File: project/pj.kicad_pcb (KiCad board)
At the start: 2 copper layers, 65 x 56.5 mm, 11 parts, among them J1 RPi_GPIO, J2 2B+, J3 zero, J4 3A+, J5 3B+, J6 4, J7 Conn_01x02, J8 Conn_01x02, SW1 SW_Push, SW2 SW_Push

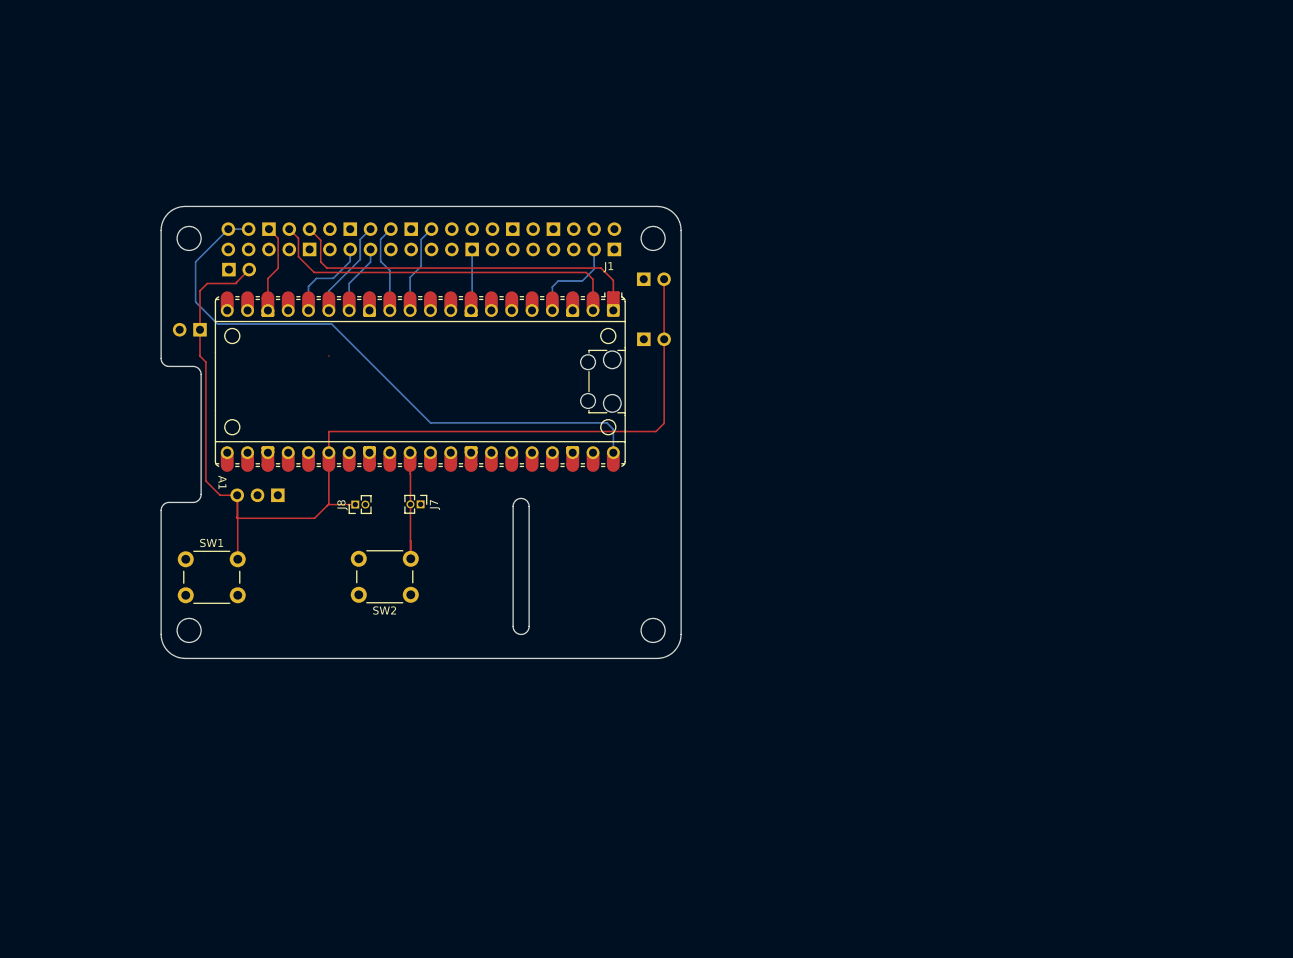
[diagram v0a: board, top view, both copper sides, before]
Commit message: ground plane on both sides
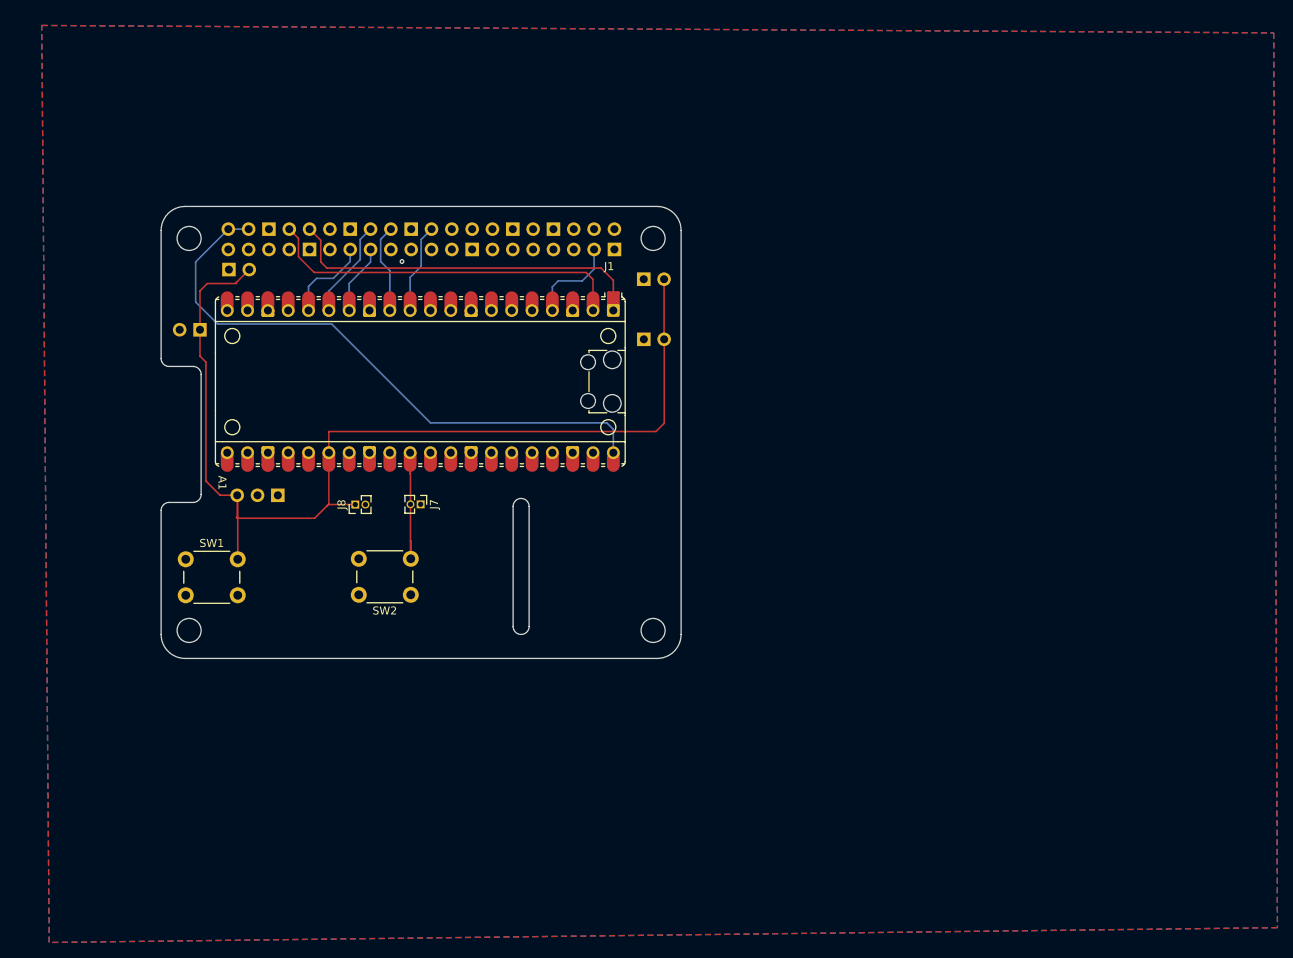
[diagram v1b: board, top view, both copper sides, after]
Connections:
- J1 pad 14: unconnected-(J1-GND-Pad14) -> GND
- J1 pad 20: unconnected-(J1-GND-Pad20) -> GND
- J1 pad 30: unconnected-(J1-GND-Pad30) -> GND
- J1 pad 34: unconnected-(J1-GND-Pad34) -> GND
- J1 pad 9: unconnected-(J1-GND-Pad9) -> GND
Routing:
- net GND: track 18.9 -> 0.19 mm, vias 0 -> 1
- added copper zone on B.Cu, net GND
- added copper zone on F.Cu, net GND

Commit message: pwr eneble
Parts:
- added J10: Pico PWR enable, Jumper:SolderJumper-2_P1.3mm_Bridged2Bar_Pad1.0x1.5mm, F.Cu at (93.0, 77.5)
- added J9: External PWR, Connector_PinHeader_1.27mm:PinHeader_1x02_P1.27mm_Vertical, F.Cu at (93.0, 83.2)
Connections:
- J1 pad 2: Net-(A1-VBUS) -> Net-(J10-Pin_2)
- J1 pad 4: Net-(A1-VBUS) -> Net-(J10-Pin_2)
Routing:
- net Net-(A1-VBUS): track 75.1 -> 6.24 mm
- net Net-(A1-GPIO20): track 132.2 -> 91.3 mm
- net Net-(J10-Pin_2): track 0.00 -> 4.46 mm
- removed copper zone on B.Cu, net GND
- removed copper zone on F.Cu, net GND

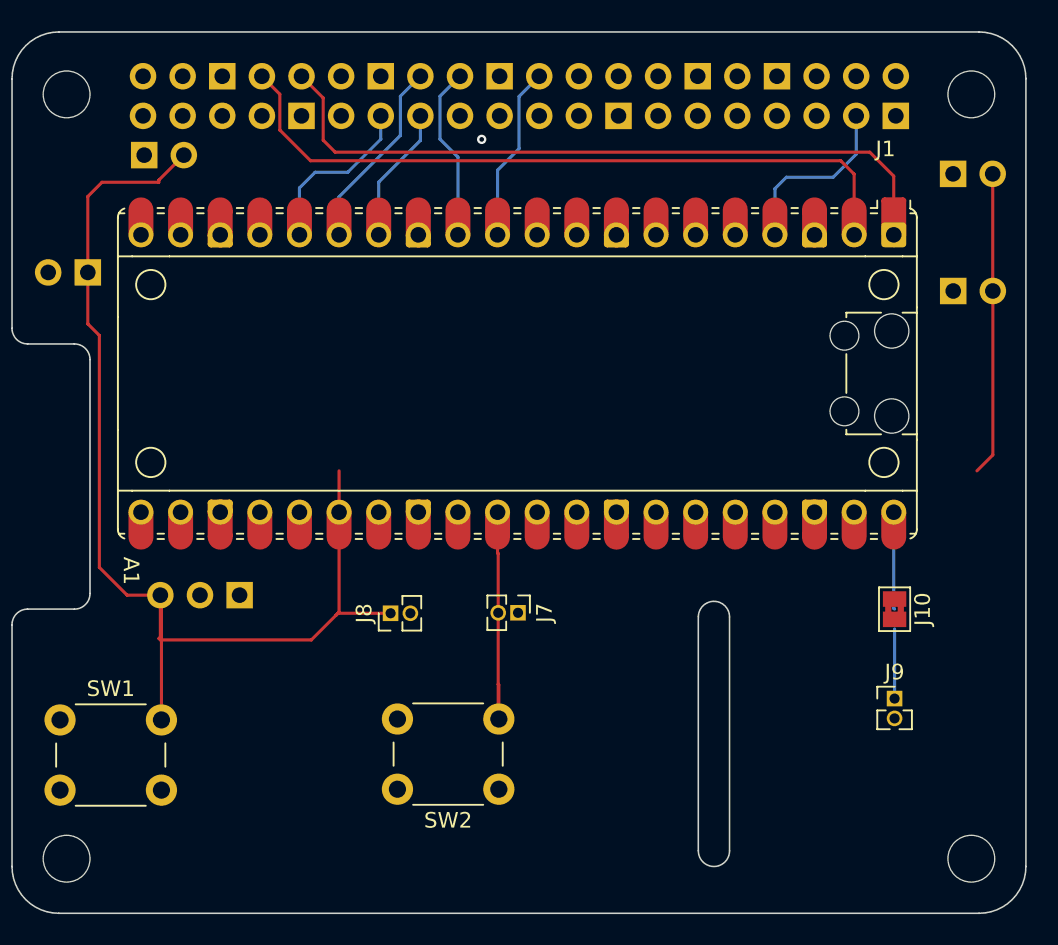
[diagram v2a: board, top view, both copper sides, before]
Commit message: re-route power for more power
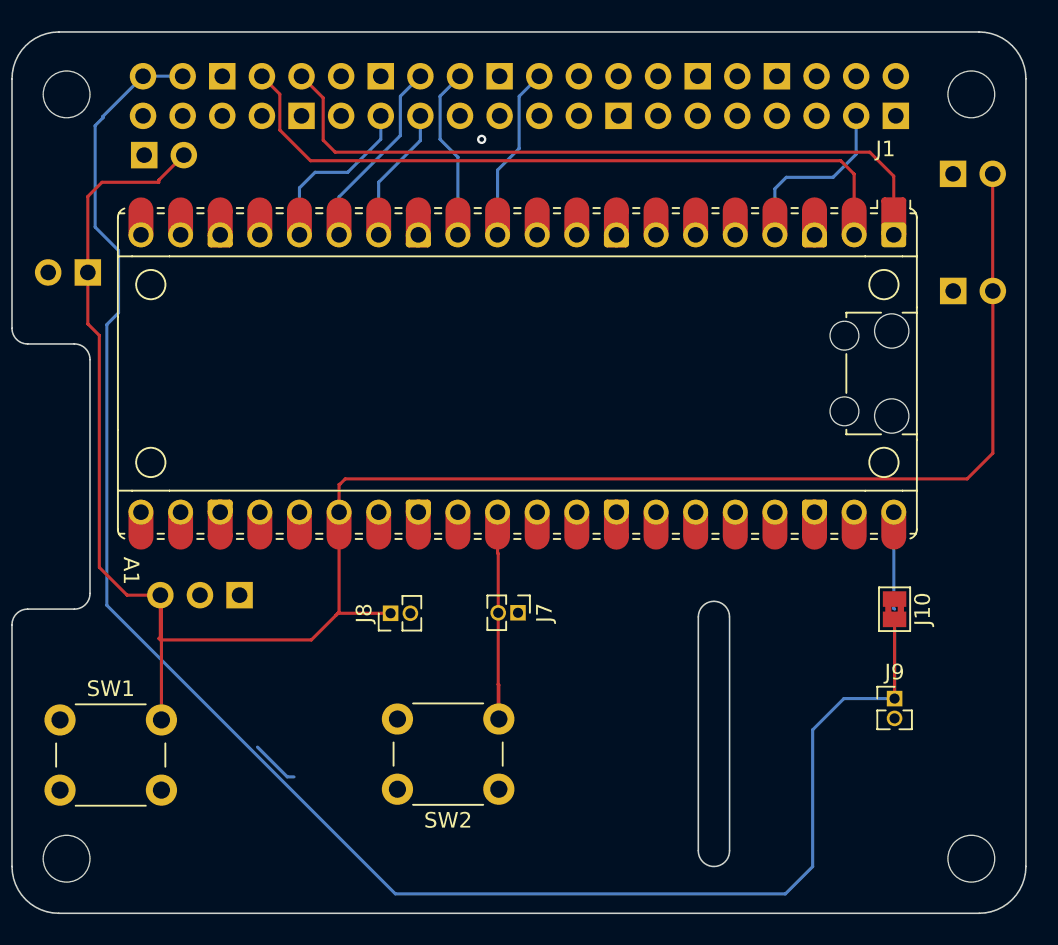
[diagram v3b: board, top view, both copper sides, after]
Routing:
- net Net-(J10-Pin_2): track 4.46 -> 116.7 mm
- net Net-(A1-GPIO20): track 91.3 -> 131.6 mm
- net (no net): track 0.00 -> 3.13 mm
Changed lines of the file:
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@@
 		(fp_arc
 			(start 10.579676 25.189937)
-			(mid 10.35796 25.493961)
+			(mid 10.357949 25.493953)
 			(end 10 25.61)
 			(stroke
@@
 	)
 	(segment
+		(start 54.065686 88.25)
+		(end 52.157843 86.342157)
+		(width 0.2)
+		(layer "B.Cu")
+		(net 0)
+	)
+	(segment
+		(start 54.5 88.25)
+		(end 54.065686 88.25)
+		(width 0.2)
+		(layer "B.Cu")
+		(net 0)
+	)
+	(segment
 		(start 67.46 53.4125)
 		(end 67.5475 53.5)
@@
 	)
 	(segment
+		(start 57.3875 71.28)
+		(end 57.3875 69.5)
+		(width 0.2)
+		(layer "F.Cu")
+		(net 10)
+	)
+	(segment
 		(start 45.93 79.47)
 		(end 45.84 79.38)
@@
 	)
 	(segment
-		(start 57.3875 71.28)
-		(end 57.3875 68.63)
+		(start 55.61 79.47)
+		(end 45.93 79.47)
 		(width 0.2)
 		(layer "F.Cu")
@@
 	)
 	(segment
-		(start 55.61 79.47)
-		(end 45.93 79.47)
+		(start 41.28 55.91)
+		(end 41.28 51.04)
 		(width 0.2)
 		(layer "F.Cu")
@@
 	)
 	(segment
-		(start 41.28 55.91)
-		(end 41.28 51.04)
+		(start 57.783778 69.146278)
+		(end 97.653722 69.146278)
 		(width 0.2)
 		(layer "F.Cu")
@@
 	)
 	(segment
+		(start 57.3875 69.5)
+		(end 57.430056 69.5)
+		(width 0.2)
+		(layer "F.Cu")
+		(net 10)
+	)
+	(segment
+		(start 97.653722 69.146278)
+		(end 99.3 67.5)
+		(width 0.2)
+		(layer "F.Cu")
+		(net 10)
+	)
+	(segment
 		(start 45.83 50.13)
 		(end 45.83 49.995)
@@
 	)
 	(segment
+		(start 99.3 57.1)
+		(end 99.3 67.5)
+		(width 0.2)
+		(layer "F.Cu")
+		(net 10)
+	)
+	(segment
 		(start 41.28 59.21)
 		(end 42.02 59.95)
@@
 	)
 	(segment
-		(start 99.3 57.1)
-		(end 99.3 67.61)
-		(width 0.2)
-		(layer "F.Cu")
-		(net 10)
-	)
-	(segment
 		(start 43.8 76.6)
 		(end 45.93 76.6)
@@
 	)
 	(segment
-		(start 57.3875 77.6925)
-		(end 57.18 77.9)
+		(start 57.430056 69.5)
+		(end 57.783778 69.146278)
 		(width 0.2)
 		(layer "F.Cu")
@@
 	)
 	(segment
-		(start 99.3 67.61)
-		(end 98.28 68.63)
+		(start 57.3875 77.6925)
+		(end 57.18 77.9)
 		(width 0.2)
 		(layer "F.Cu")
@@
 	)
 	(segment
+		(start 93 78.15)
+		(end 93 83.23)
+		(width 0.2)
+		(layer "F.Cu")
+		(net 63)
+	)
+	(segment
+		(start 43.25 58.5)
+		(end 42.5 59.25)
+		(width 0.2)
+		(layer "B.Cu")
+		(net 63)
+	)
+	(segment
+		(start 44.82 43.333)
+		(end 47.36 43.333)
+		(width 0.2)
+		(layer "B.Cu")
+		(net 63)
+	)
+	(segment
+		(start 43.25 54.5)
+		(end 43.25 58.5)
+		(width 0.2)
+		(layer "B.Cu")
+		(net 63)
+	)
+	(segment
+		(start 89.75 83.23)
+		(end 93 83.23)
+		(width 0.2)
+		(layer "B.Cu")
+		(net 63)
+	)
+	(segment
+		(start 41.75 53)
+		(end 43.25 54.5)
+		(width 0.2)
+		(layer "B.Cu")
+		(net 63)
+	)
+	(segment
+		(start 42.25 45.903)
+		(end 42.25 46)
+		(width 0.2)
+		(layer "B.Cu")
+		(net 63)
+	)
+	(segment
+		(start 61 95.75)
+		(end 86 95.75)
+		(width 0.2)
+		(layer "B.Cu")
+		(net 63)
+	)
+	(segment
+		(start 44.82 43.333)
+		(end 42.25 45.903)
+		(width 0.2)
+		(layer "B.Cu")
+		(net 63)
+	)
+	(segment
+		(start 87.75 94)
+		(end 87.75 85.23)
+		(width 0.2)
+		(layer "B.Cu")
+		(net 63)
+	)
+	(segment
+		(start 87.75 85.23)
+		(end 89.75 83.23)
+		(width 0.2)
+		(layer "B.Cu")
+		(net 63)
+	)
+	(segment
+		(start 42.5 77.25)
+		(end 61 95.75)
+		(width 0.2)
+		(layer "B.Cu")
+		(net 63)
+	)
+	(segment
+		(start 86 95.75)
+		(end 87.75 94)
+		(width 0.2)
+		(layer "B.Cu")
+		(net 63)
+	)
+	(segment
+		(start 42.5 59.25)
+		(end 42.5 77.25)
+		(width 0.2)
+		(layer "B.Cu")
+		(net 63)
+	)
+	(segment
+		(start 42.25 46)
+		(end 41.75 46.5)
+		(width 0.2)
+		(layer "B.Cu")
+		(net 63)
+	)
+	(segment
 		(start 93 78.77)
 		(end 93 83.23)
 		(width 0.2)
 		(layer "B.Cu")
+		(net 63)
+	)
+	(segment
+		(start 41.75 46.5)
+		(end 41.75 53)
+		(width 0.2)
+		(layer "B.Cu")

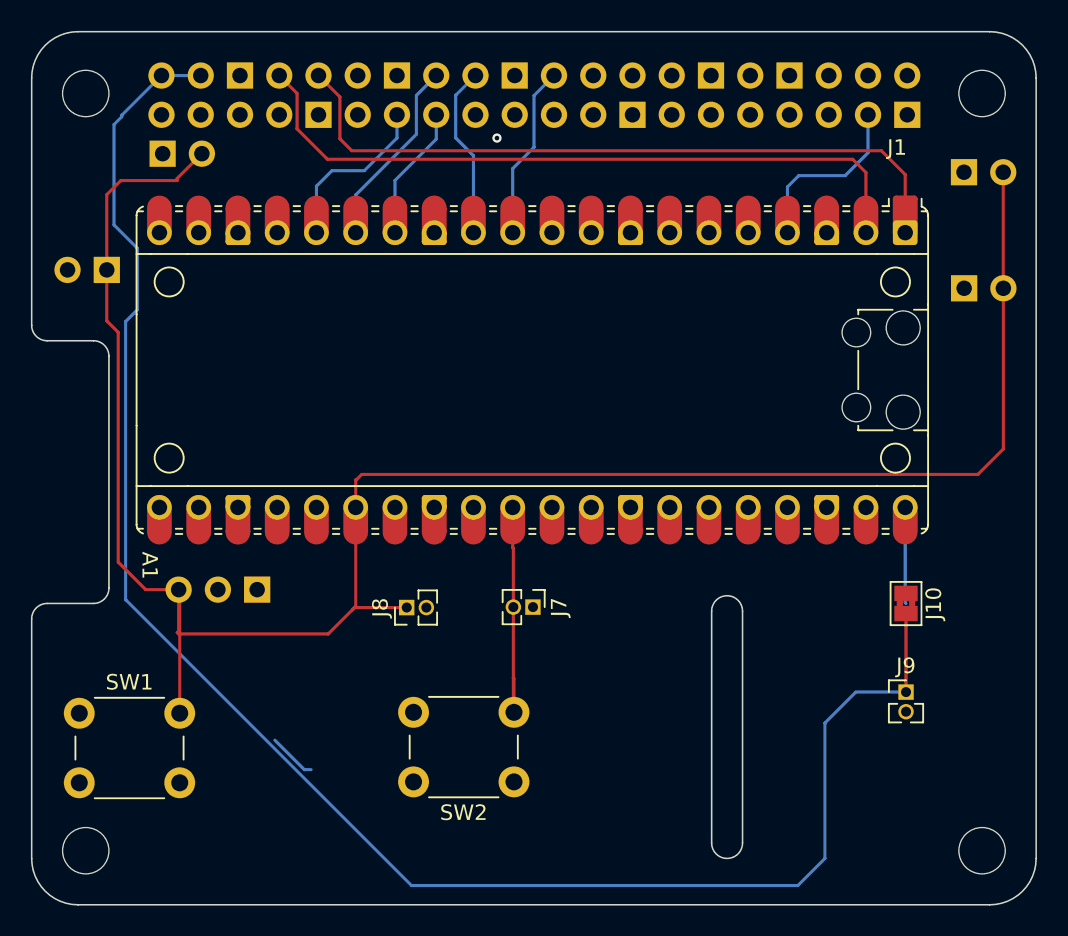
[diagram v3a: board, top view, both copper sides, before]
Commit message: tweek the RUN holes
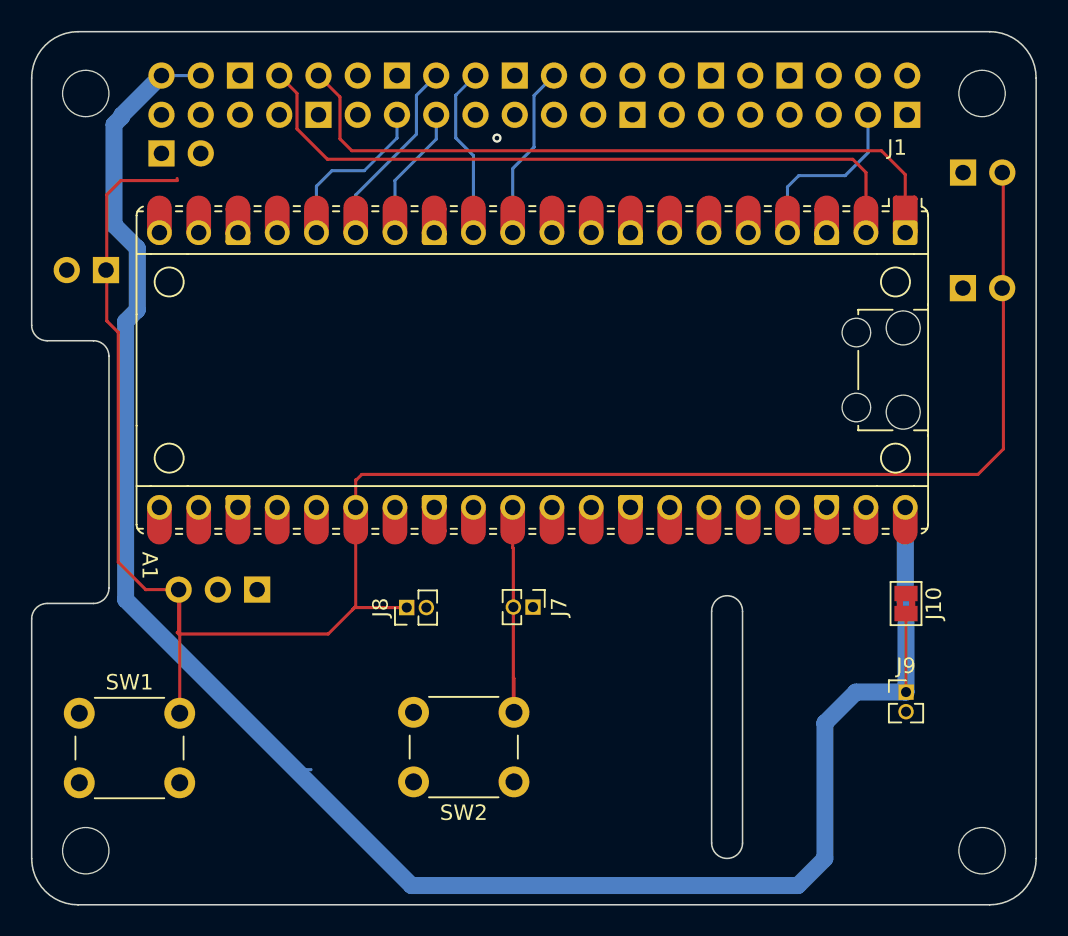
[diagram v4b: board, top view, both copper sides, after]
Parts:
- moved J5 0.08 mm to (96.7, 57.1)
- moved J3 0.08 mm to (44.8, 48.4)
- moved J4 0.06 mm to (96.7, 49.6)
- moved J2 0.05 mm to (41.2, 55.9)
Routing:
- net (no net): track 3.13 -> 0.00 mm
- net Net-(J10-Pin_2): track 116.7 -> 119.8 mm
- net Net-(A1-GPIO20): track 131.6 -> 129.4 mm
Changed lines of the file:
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@@
 		(fp_arc
 			(start 10.579676 25.189937)
-			(mid 10.357949 25.493953)
+			(mid 10.357946 25.493957)
 			(end 10 25.61)
 			(stroke
@@
 	(footprint "Connector_PinHeader_2.54mm:PinHeader_1x02_P2.54mm_Vertical"
 		(layer "B.Cu")
-		(at 96.76 57.1 -90)
+		(at 96.68 57.09 -90)
 		(descr "Through hole straight pin header, 1x02, 2.54mm pitch, single row")
 		(tags "Through hole pin header THT 1x02 2.54mm single row")
@@
 	(footprint "Connector_PinHeader_2.54mm:PinHeader_1x02_P2.54mm_Vertical"
 		(layer "B.Cu")
-		(at 44.895 48.39 -90)
+		(at 44.82 48.37 -90)
 		(descr "Through hole straight pin header, 1x02, 2.54mm pitch, single row")
 		(tags "Through hole pin header THT 1x02 2.54mm single row")
@@
 	(footprint "Connector_PinHeader_2.54mm:PinHeader_1x02_P2.54mm_Vertical"
 		(layer "B.Cu")
-		(at 41.28 55.91 90)
+		(at 41.23 55.92 90)
 		(descr "Through hole straight pin header, 1x02, 2.54mm pitch, single row")
 		(tags "Through hole pin header THT 1x02 2.54mm single row")
@@
 	(footprint "Connector_PinHeader_2.54mm:PinHeader_1x02_P2.54mm_Vertical"
 		(layer "B.Cu")
-		(at 96.75 49.59 -90)
+		(at 96.69 49.61 -90)
 		(descr "Through hole straight pin header, 1x02, 2.54mm pitch, single row")
 		(tags "Through hole pin header THT 1x02 2.54mm single row")
@@
 	)
 	(segment
-		(start 54.065686 88.25)
-		(end 52.157843 86.342157)
-		(width 0.2)
-		(layer "B.Cu")
-		(net 0)
-	)
-	(segment
-		(start 54.5 88.25)
-		(end 54.065686 88.25)
-		(width 0.2)
-		(layer "B.Cu")
-		(net 0)
-	)
-	(segment
 		(start 67.46 53.4125)
 		(end 67.5475 53.5)
@@
 	)
 	(segment
-		(start 45.83 49.995)
-		(end 47.435 48.39)
-		(width 0.2)
-		(layer "F.Cu")
-		(net 10)
-	)
-	(segment
 		(start 99.29 49.59)
 		(end 99.29 57.09)
@@
 		(start 92.9475 71.28)
 		(end 92.9475 77.4475)
-		(width 0.2)
+		(width 1.1)
 		(layer "B.Cu")
 		(net 18)
@@
 	)
 	(segment
+		(start 54.065686 88.25)
+		(end 52.157843 86.342157)
+		(width 0.2)
+		(layer "B.Cu")
+		(net 63)
+	)
+	(segment
 		(start 43.25 58.5)
 		(end 42.5 59.25)
-		(width 0.2)
+		(width 1.1)
 		(layer "B.Cu")
 		(net 63)
@@
 		(start 43.25 54.5)
 		(end 43.25 58.5)
+		(width 1.1)
+		(layer "B.Cu")
+		(net 63)
+	)
+	(segment
+		(start 54.5 88.25)
+		(end 54.065686 88.25)
 		(width 0.2)
 		(layer "B.Cu")
@@
 		(start 89.75 83.23)
 		(end 93 83.23)
-		(width 0.2)
+		(width 1.1)
 		(layer "B.Cu")
 		(net 63)
@@
 		(start 41.75 53)
 		(end 43.25 54.5)
-		(width 0.2)
+		(width 1.1)
 		(layer "B.Cu")
 		(net 63)
@@
 		(start 42.25 45.903)
 		(end 42.25 46)
-		(width 0.2)
+		(width 1.1)
 		(layer "B.Cu")
 		(net 63)
@@
 		(start 61 95.75)
 		(end 86 95.75)
-		(width 0.2)
+		(width 1.1)
 		(layer "B.Cu")
 		(net 63)
@@
 		(start 44.82 43.333)
 		(end 42.25 45.903)
-		(width 0.2)
+		(width 1.1)
 		(layer "B.Cu")
 		(net 63)
@@
 		(start 87.75 94)
 		(end 87.75 85.23)
-		(width 0.2)
+		(width 1.1)
 		(layer "B.Cu")
 		(net 63)
@@
 		(start 87.75 85.23)
 		(end 89.75 83.23)
-		(width 0.2)
+		(width 1.1)
 		(layer "B.Cu")
 		(net 63)
@@
 		(start 42.5 77.25)
 		(end 61 95.75)
-		(width 0.2)
+		(width 1.1)
 		(layer "B.Cu")
 		(net 63)
@@
 		(start 86 95.75)
 		(end 87.75 94)
-		(width 0.2)
+		(width 1.1)
 		(layer "B.Cu")
 		(net 63)
@@
 		(start 42.5 59.25)
 		(end 42.5 77.25)
-		(width 0.2)
+		(width 1.1)
 		(layer "B.Cu")
 		(net 63)
@@
 		(start 42.25 46)
 		(end 41.75 46.5)
-		(width 0.2)
+		(width 1.1)
 		(layer "B.Cu")
 		(net 63)
@@
 		(start 93 78.77)
 		(end 93 83.23)
-		(width 0.2)
+		(width 1.1)
 		(layer "B.Cu")
 		(net 63)
@@
 		(start 41.75 46.5)
 		(end 41.75 53)
-		(width 0.2)
+		(width 1.1)
 		(layer "B.Cu")
 		(net 63)
